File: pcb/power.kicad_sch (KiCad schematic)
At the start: 13 parts

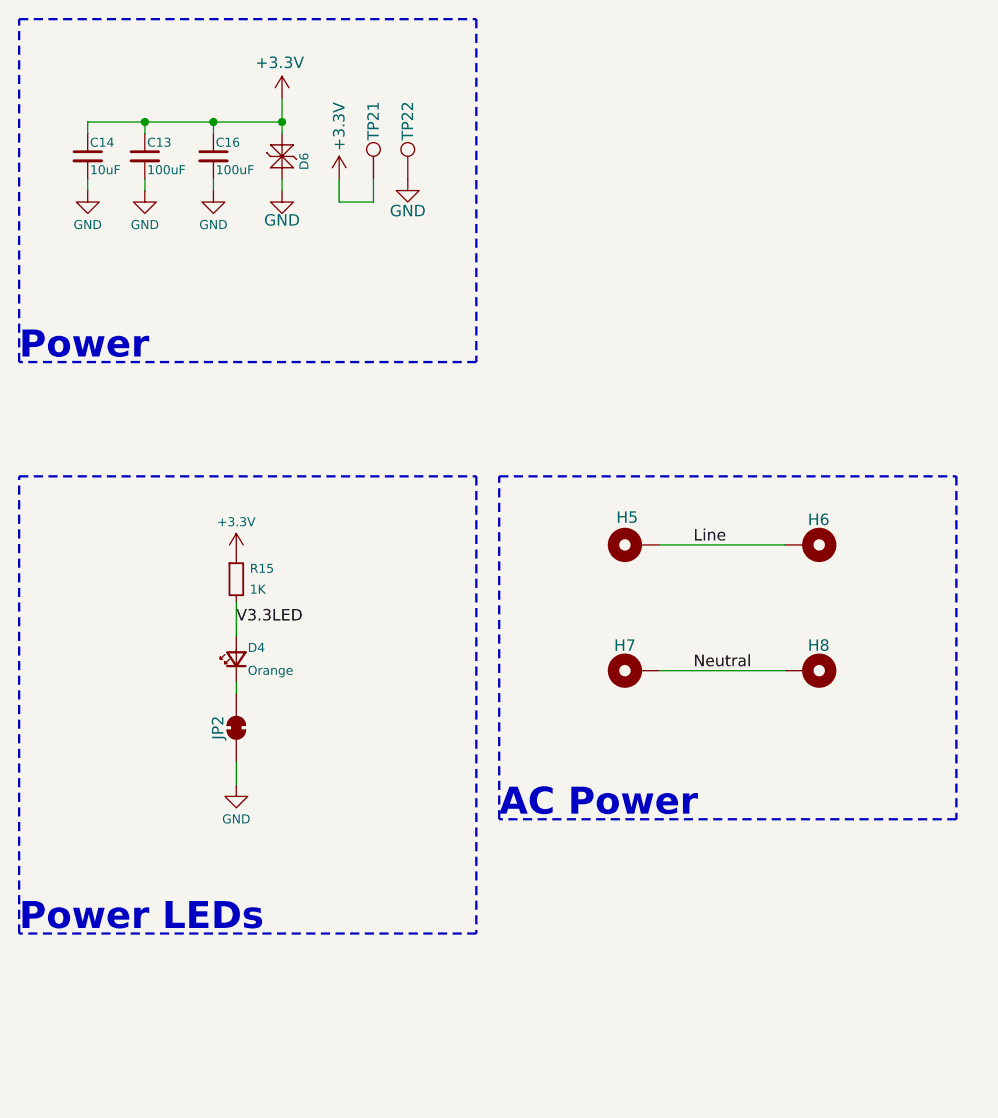
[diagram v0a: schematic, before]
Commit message: refactored to STM32
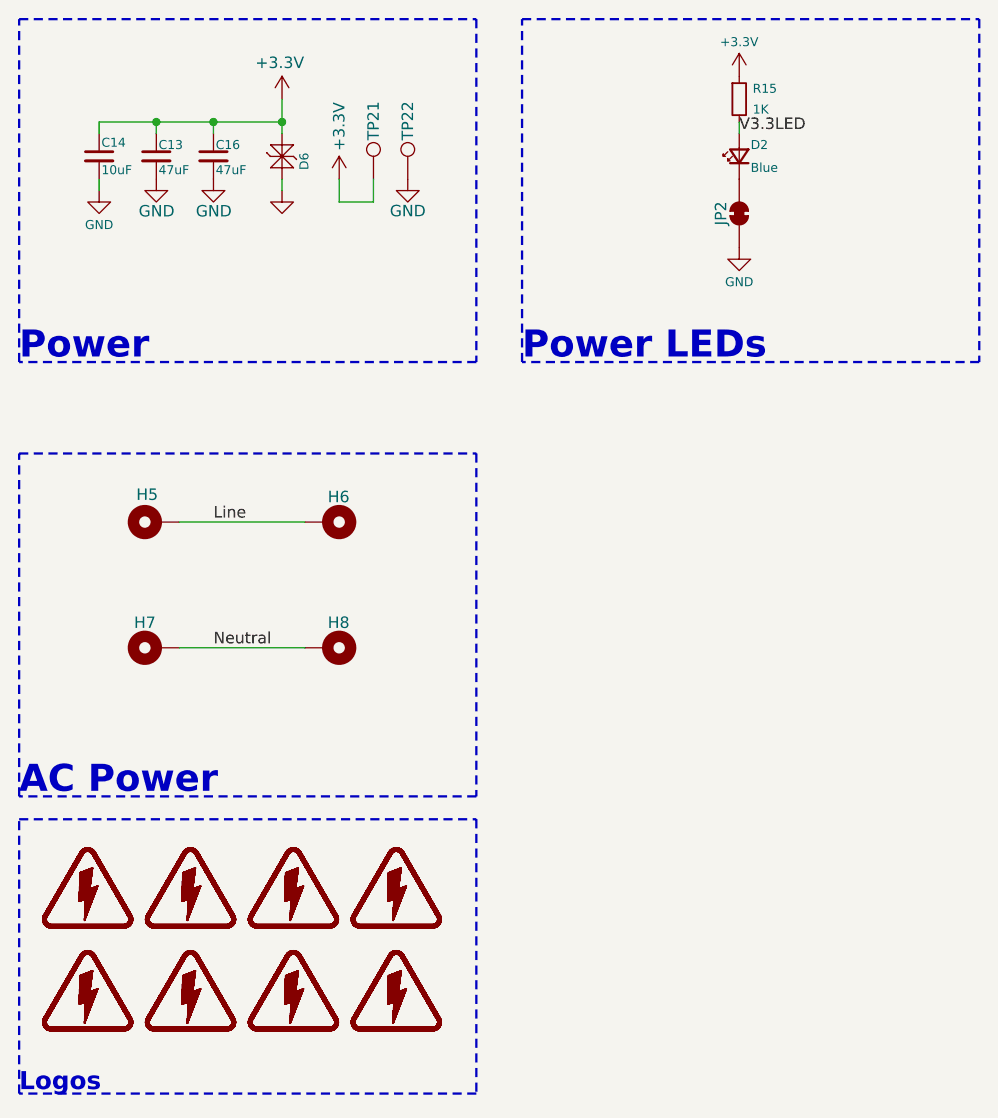
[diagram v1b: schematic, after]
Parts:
- removed C13, C16: 100uF, CRGM Passive:C_1206_3216Metric, symbol Device:C_Small
- removed D4: Orange, CRGM Passive:LED_0603_1608Metric, symbol Device:LED_Small
- added C13, C16: 47uF, CRGM Passive:C_0805_2012Metric, symbol CRGM Passive:C_Small
- added D2: Blue, CRGM Passive:LED_0603_1608Metric, symbol Device:LED_Small
- added SYM1, SYM2, SYM3, SYM4, SYM5, SYM6, SYM7, SYM8: (no value), CRGM Symbols:HIGH-VOLTAGE-5MM, symbol CRGM Symbols:High Voltage
- H5, H6, H7, H8, JP2, TP21, TP22: value ~ -> (none)
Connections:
- net +3.3V: now also C13.1, C16.1
- net GND: now also C13.2, C16.2
- net V3.3LED: now also D2.2 (A)
- net at JP2.2 (B): now also D2.1 (K)
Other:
- note added: "Logos"
- moved on the sheet: C14, H5, H6, H7, H8, JP2, R15

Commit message: Added additional silkscreen to AC side
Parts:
- removed D2: Blue, CRGM Passive:LED_0603_1608Metric, symbol Device:LED_Small
- added D2: Blue, CRGM Passive:LED_0603_1608Metric, symbol CRGM Passive:LED_Small
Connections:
- net V3.3LED: now also D2.2 (A)
- net at JP2.2 (B): now also D2.1 (K)

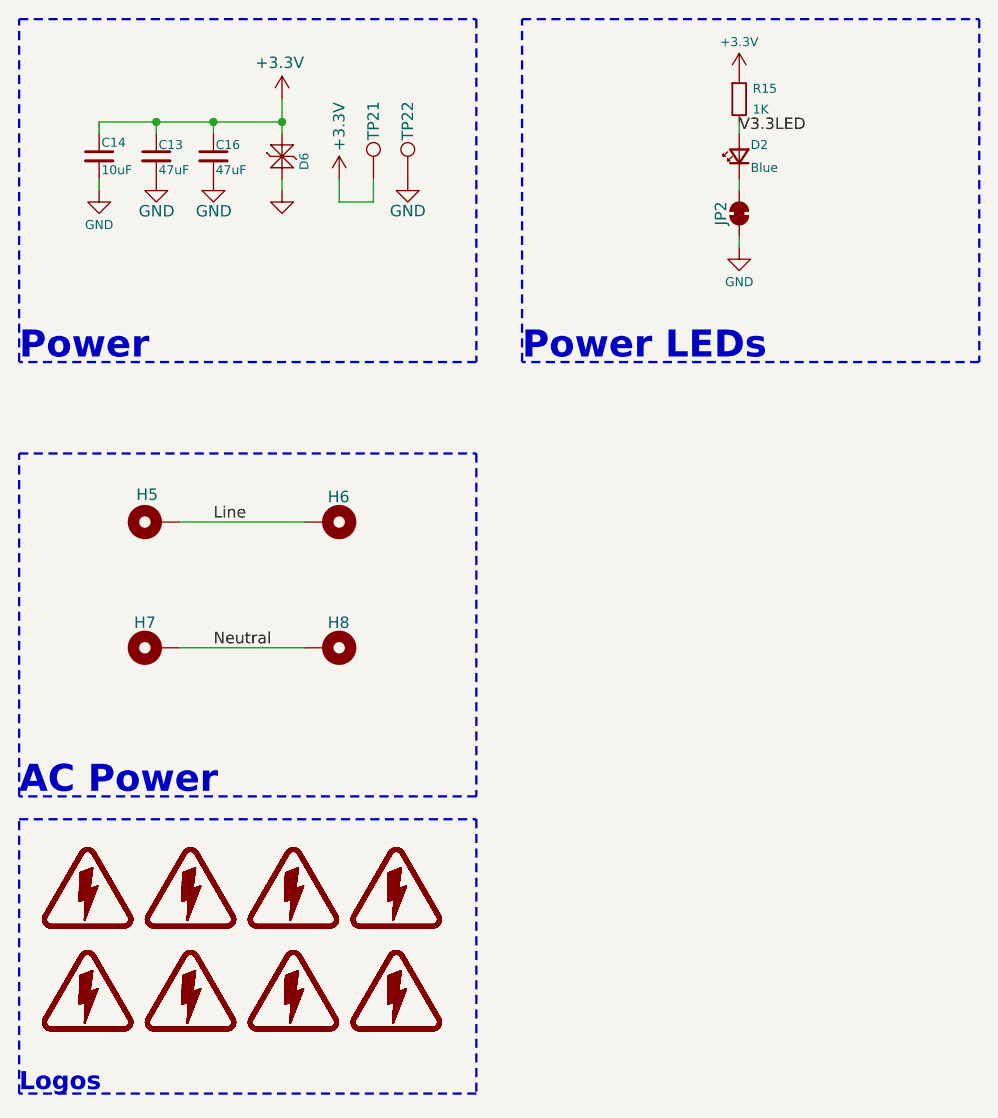
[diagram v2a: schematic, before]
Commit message: Removed AC input via copper
Testing revealed sending AC through copper did not trigger device. Removed ability to send AC through the PCB.
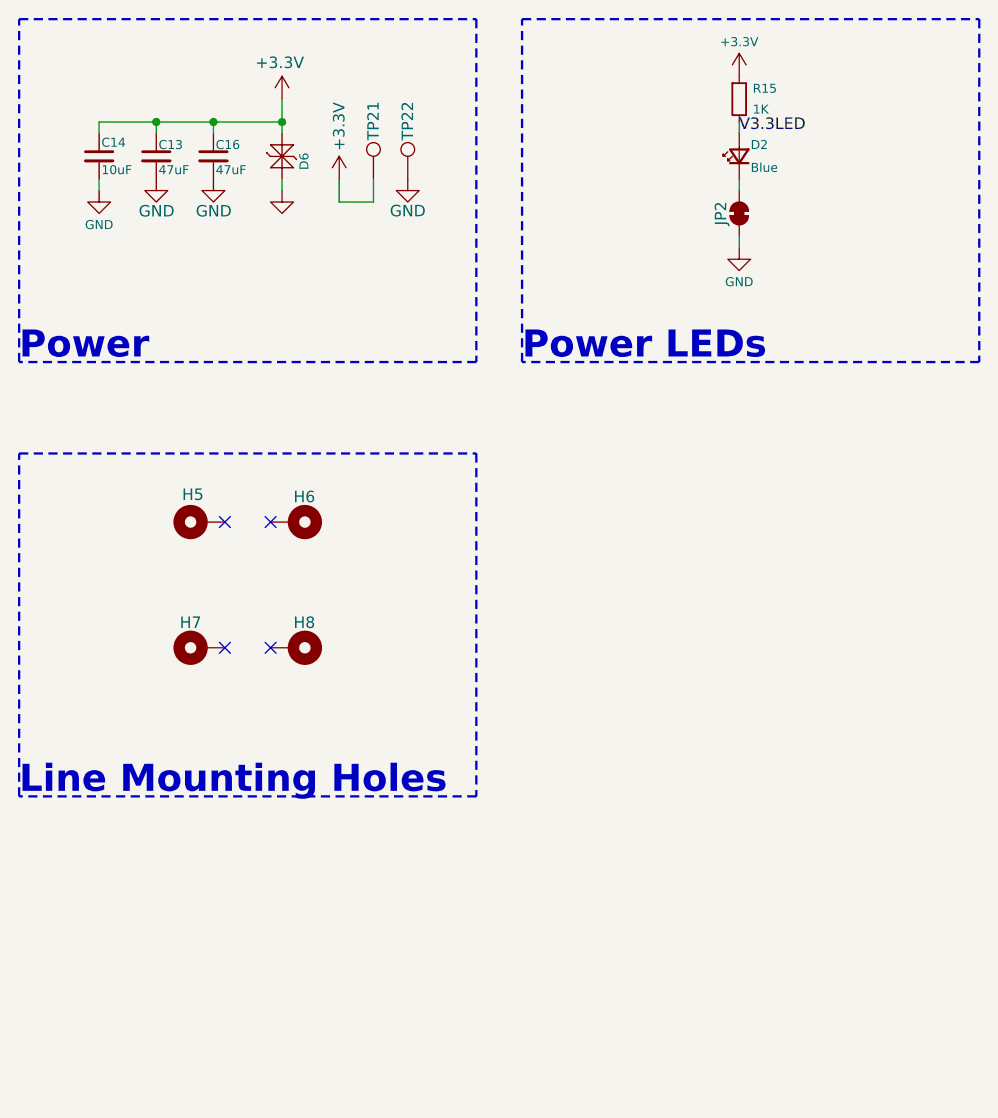
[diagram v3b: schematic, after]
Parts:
- removed SYM1, SYM2, SYM3, SYM4, SYM5, SYM6, SYM7, SYM8: (no value), CRGM Symbols:HIGH-VOLTAGE-5MM, symbol CRGM Symbols:High Voltage
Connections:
- net Line: no longer names the net of H5.1
- net Line: no longer H6.1
- net Neutral: no longer names the net of H7.1
- net Neutral: no longer H8.1
- no-connect marks 0 -> 4
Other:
- note added: "Line Mounting Holes"
- note removed: "AC Power"
- note removed: "Logos"
- moved on the sheet: H5, H6, H7, H8
